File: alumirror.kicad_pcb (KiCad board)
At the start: 2 copper layers, 152.4 x 90.3 mm, 56 parts, among them SW00 PG1350, SW01 PG1350, SW02 PG1350, SW03 PG1350, SW04 PG1350, SW05 PG1350, SW10 PG1350, SW11 PG1350, SW12 PG1350, SW13 PG1350, SW14 PG1350, SW15 PG1350, SW20 PG1350, SW21 PG1350, SW22 PG1350, SW23 PG1350, SW24 PG1350, SW25 PG1350, SW30 PG1350, SW31 PG1350/SKQUCAA010, U1 CH552T, U2 CH552T

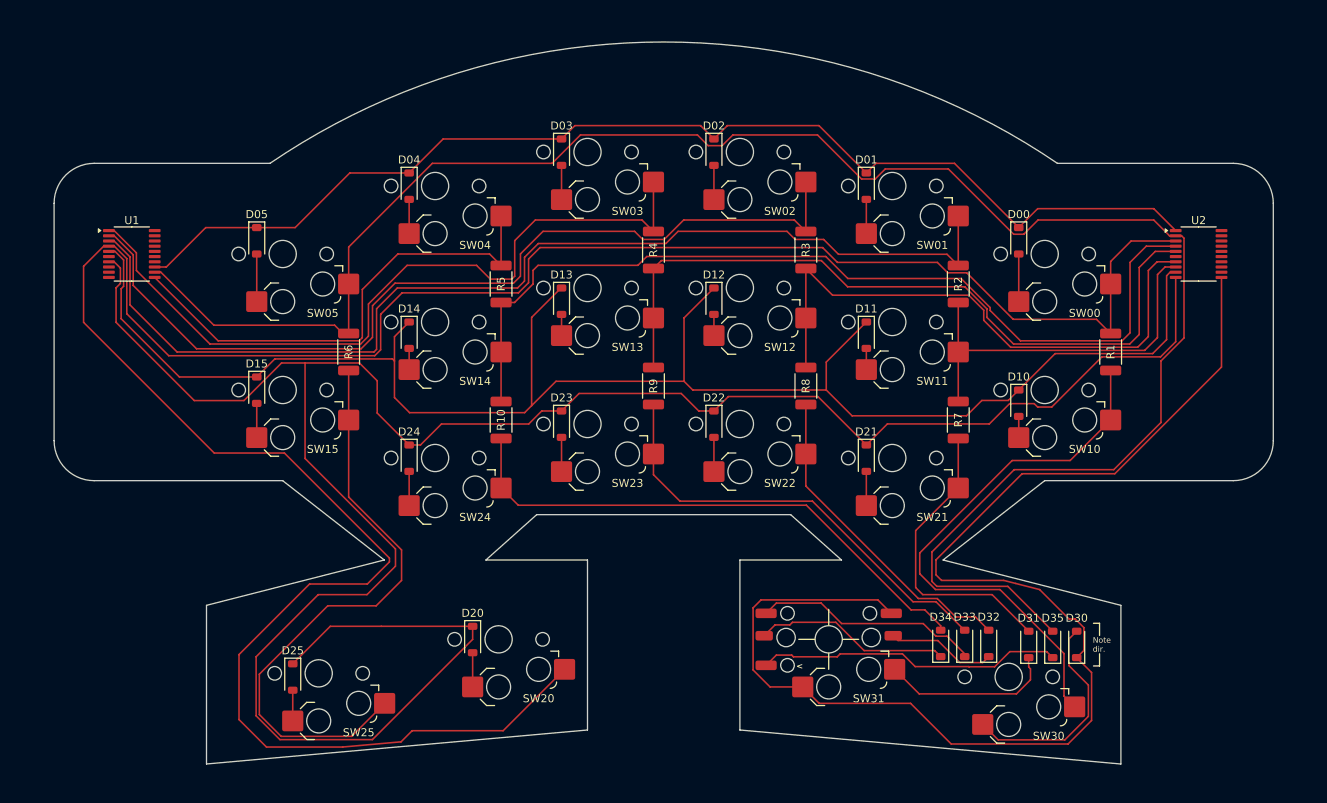
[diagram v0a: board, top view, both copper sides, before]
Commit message: Move bottom row one column over
This allows the left thumb keys to be on adjacent columns and saves routing Column 0 all the way across the board.
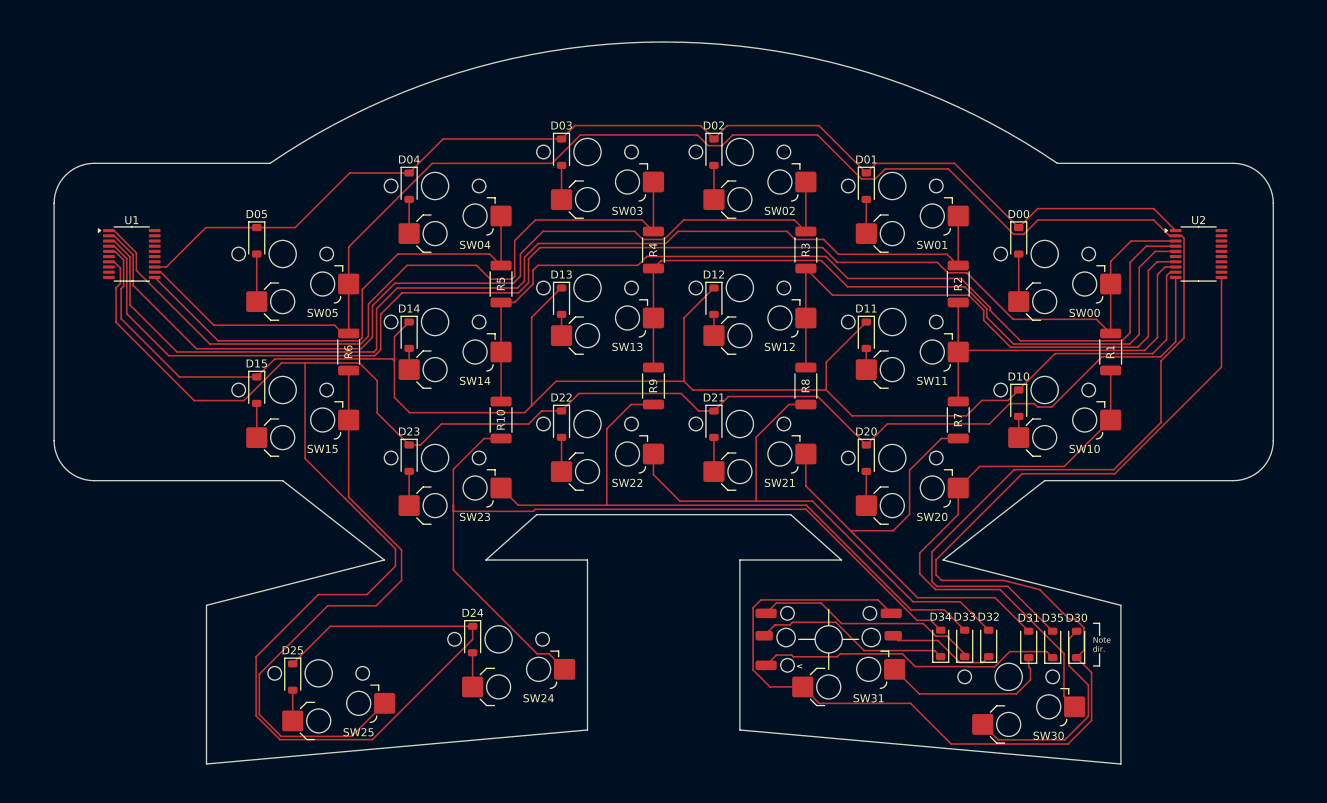
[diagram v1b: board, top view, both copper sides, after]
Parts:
- renumbered D21 to D20, D22 to D21, D23 to D22, D24 to D23, D20 to D24, SW21 to SW20, SW22 to SW21, SW23 to SW22, SW24 to SW23, SW20 to SW24
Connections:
- SW20 pad 1: /Col1R' -> /Col0'
- SW21 pad 1: /Col2R' -> /Col1R'
- SW22 pad 1: /Col3R' -> /Col2R'
- SW23 pad 1: /Col4R' -> /Col3R'
- SW24 pad 1: Col0 -> /Col4R'
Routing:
- net Col0: track 307.3 -> 167.5 mm
- net /Col4R': track 68.4 -> 107.2 mm
- net /Col2R': track 40.5 -> 68.4 mm
- net /Col3R': track 55.7 -> 82.0 mm
- net /Col1R': track 37.2 -> 60.8 mm
- net /Col0': track 68.9 -> 70.9 mm

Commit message: Tidy routing
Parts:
- moved R7 5.50 mm to (183.7, 73.2)
- moved R9 5.50 mm to (145.6, 68.9)
- moved R10 5.49 mm to (126.6, 73.2)
- moved R8 5.49 mm to (164.7, 68.9)
- moved D23 1.67 mm to (120.6, 76.3)
- moved D20 1.67 mm to (177.7, 76.3)
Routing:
- net Row2: track 293.5 -> 227.3 mm
- net /Col1R': track 60.8 -> 50.1 mm
- net /Col2R': track 68.4 -> 61.6 mm
- net /Col4R': track 107.2 -> 102.1 mm
- net /Col3R': track 82.0 -> 78.0 mm
- net /Col5': track 75.2 -> 72.1 mm
- net Col4R: track 114.7 -> 116.8 mm
- net Col3R: track 92.2 -> 94.2 mm
- net Col2R: track 72.7 -> 74.8 mm
- net Net-(D23-A): track 4.28 -> 5.95 mm
- net Net-(D20-A): track 4.28 -> 5.95 mm
- net Col1R: track 48.5 -> 50.2 mm

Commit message: Tidy schematic
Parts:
- SW25, SW30: value PG1350 -> PG1350_1½U
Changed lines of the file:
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@@
 			)
 		)
-		(property "Value" "PG1350"
+		(property "Value" "PG1350_1½U"
 			(at 0 0 180)
 			(layer "F.Fab")
@@
 			)
 		)
-		(property "Value" "PG1350"
+		(property "Value" "PG1350_1½U"
 			(at 0 0 180)
 			(layer "F.Fab")

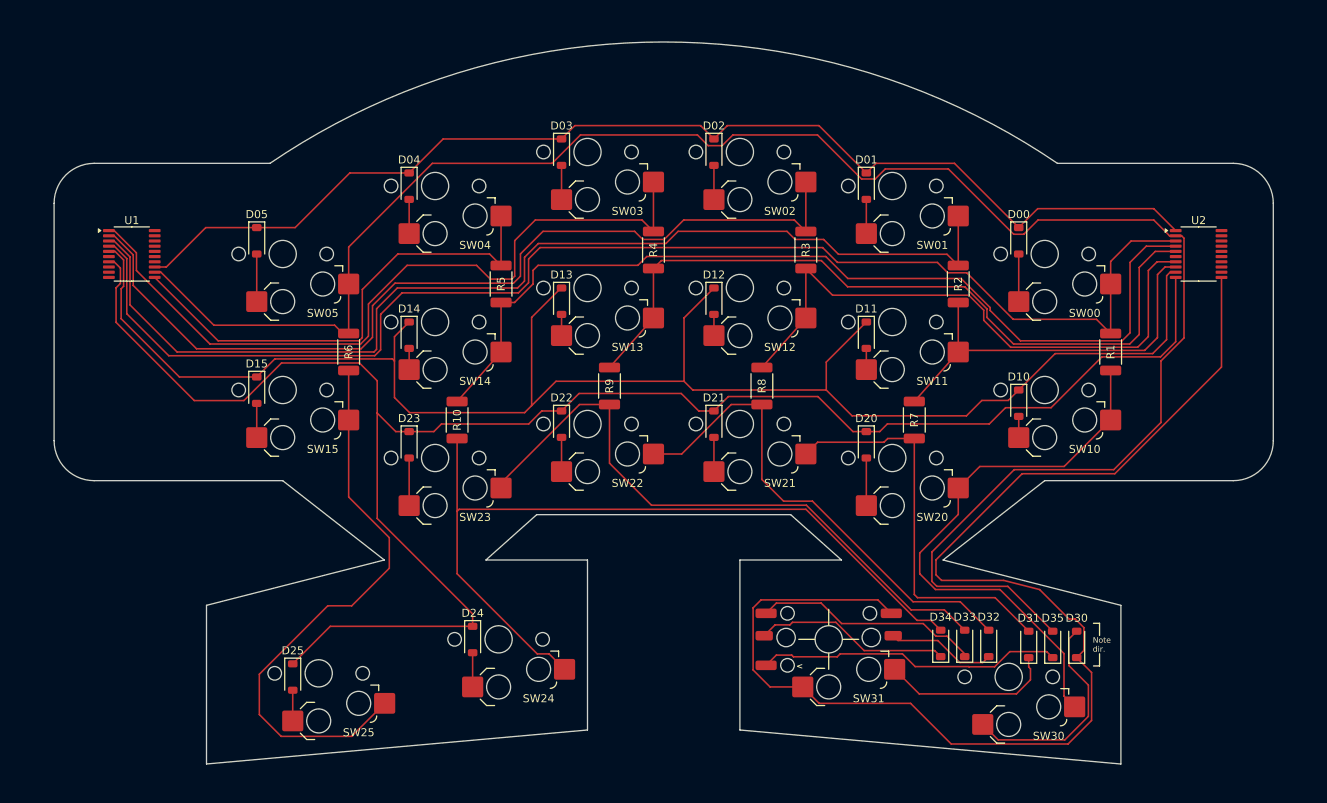
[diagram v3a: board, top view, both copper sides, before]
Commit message: Add lefthand active components to PCB and route
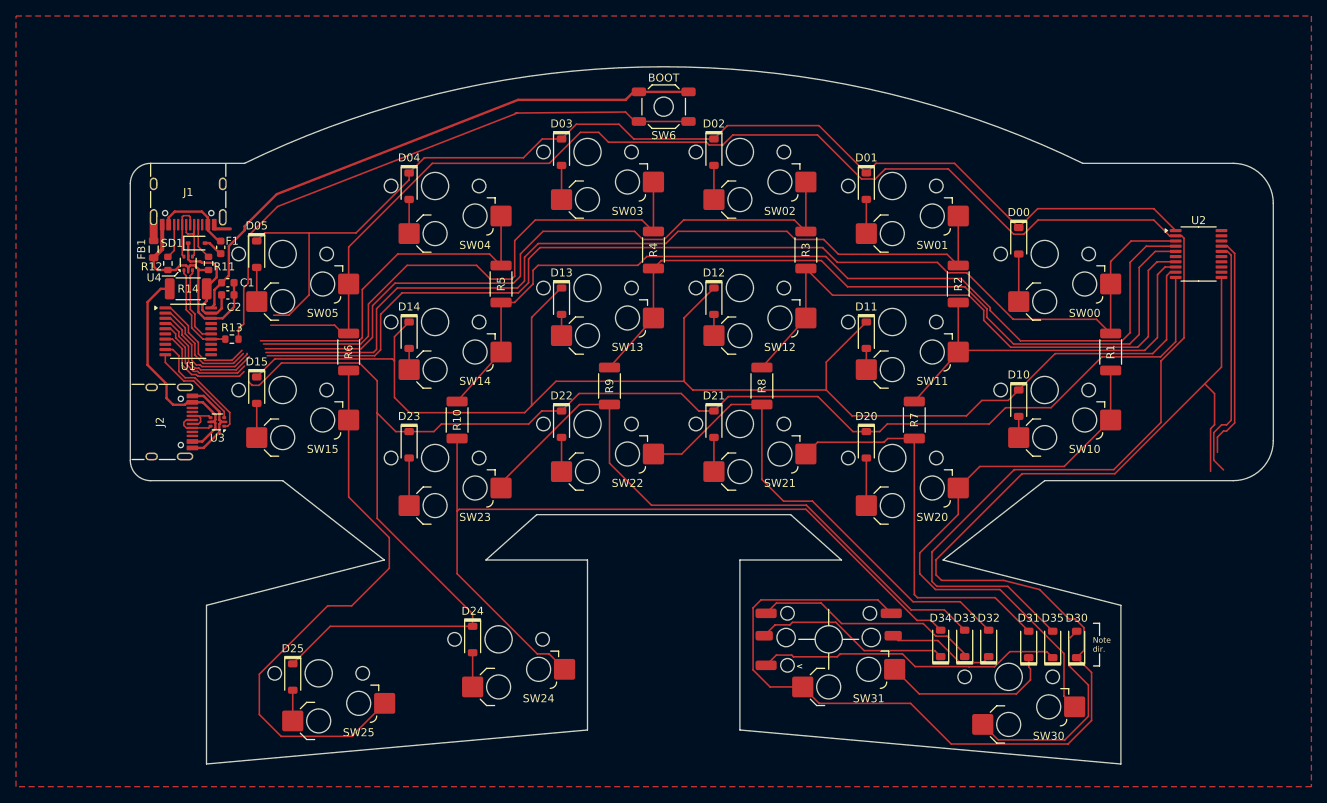
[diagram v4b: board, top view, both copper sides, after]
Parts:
- added C1: 100nF, Capacitor_SMD:C_0603_1608Metric, F.Cu at (97.9, 56.0)
- added C2: 100nF, Capacitor_SMD:C_0603_1608Metric, F.Cu at (97.9, 57.5)
- added F1: 500mA, Fuse:Fuse_0603_1608Metric, F.Cu at (97.0, 51.6)
- added FB1: FerriteBead, Inductor_SMD:L_0805_2012Metric, F.Cu at (88.6, 51.8)
- added J1: USB_C_Receptacle_USB2.0_16P_2SH, Project Library:USB_C_Receptacle_HRO_TYPE-C-31-M-12, F.Cu at (93.0, 44.7)
- added J2: USB_C_Receptacle_USB2.0_16P_2SH, Project Library:USB_C_Receptacle_HRO_TYPE-C-31-M-12, F.Cu at (89.4, 73.4)
- added NT1: NetTie_2, Project Library:NetTie-2_SMD_Pad0.2mm, F.Cu at (96.7, 63.1)
- added R11: 5k1, Resistor_SMD:R_0603_1608Metric, F.Cu at (95.5, 53.6)
- added R12: 5k1, Resistor_SMD:R_0603_1608Metric, F.Cu at (90.4, 53.6)
- added R13: 10k, Resistor_SMD:R_0603_1608Metric, F.Cu at (98.4, 63.1)
- added R14: 0R, Project Library:R_2010_5025Metric_Mod, F.Cu at (93.0, 56.8)
- added SD1: PMEG2010EA, Diode_SMD:D_SOD-323, F.Cu at (94.0, 51.1)
- added SW6: BOOT, Project Library:SW_SPST_SKQG_WithStem, F.Cu at (152.4, 34.0)
- added U3: USBLC6-2P6, Package_TO_SOT_SMD:SOT-666, F.Cu at (96.6, 73.4)
- added U4: USBLC6-2P6, Package_TO_SOT_SMD:SOT-666, F.Cu at (93.0, 53.6)
- moved U1 12.0 mm to (93.0, 62.1)
- moved D05 1.67 mm to (101.5, 52.4)
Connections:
- U1 pad 14: unconnected-(U1-P3.6/UDP-Pad14) -> USB_L+
- U1 pad 15: unconnected-(U1-P3.7/UDM-Pad15) -> USB_L-
- U1 pad 18: unconnected-(U1-GND-Pad18) -> GND
- U1 pad 19: unconnected-(U1-VCC-Pad19) -> VCC_L
- U1 pad 20: unconnected-(U1-V33-Pad20) -> +3V3_L
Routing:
- net Net-(R13-Pad2): track 0.00 -> 72.9 mm
- net +3V3_L: track 0.00 -> 71.7 mm
- net GND: track 0.00 -> 41.1 mm
- net VCC_L': track 0.00 -> 30.0 mm
- net TX_R: track 0.00 -> 30.0 mm
- net RX_R: track 0.00 -> 28.0 mm
- net Col5: track 238.1 -> 221.1 mm
- net Row2: track 227.3 -> 210.5 mm
- net VCC_L: track 0.00 -> 16.7 mm
- net Col4L: track 61.4 -> 44.9 mm
- net Row1: track 212.2 -> 196.4 mm
- net TX_L: track 0.00 -> 14.7 mm
- net Col0: track 167.5 -> 153.1 mm
- net Col1L: track 134.3 -> 120.5 mm
- net Col2L: track 113.5 -> 100.0 mm
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- added copper zone on F.Cu, net GND
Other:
- board size 152.4 x 90.3 mm -> 142.9 x 87.2 mm

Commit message: Renamed all key switches to K##
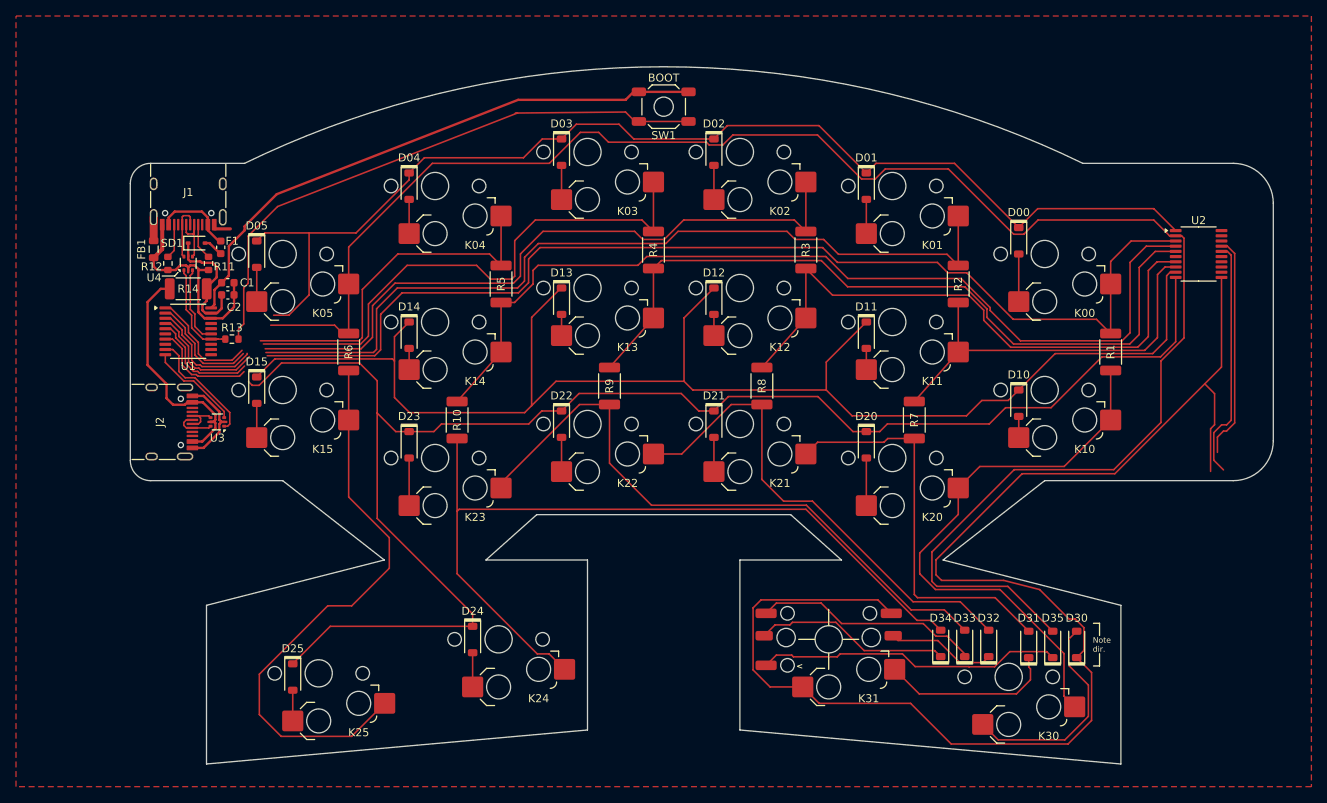
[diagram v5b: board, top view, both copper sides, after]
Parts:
- renumbered SW00 to K00, SW01 to K01, SW02 to K02, SW03 to K03, SW04 to K04, SW05 to K05, SW10 to K10, SW11 to K11, SW12 to K12, SW13 to K13, SW14 to K14, SW15 to K15, SW20 to K20, SW21 to K21, SW22 to K22, SW23 to K23, SW24 to K24, SW25 to K25, SW30 to K30, SW31 to K31, SW6 to SW1
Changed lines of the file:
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@@
 		(at 104.775 69.416683)
 		(descr "Hotswap footprint for Kailh Choc style switches")
-		(property "Reference" "SW15"
+		(property "Reference" "K15"
 			(at 5 7.4 180)
 			(layer "F.SilkS")
@@
 		(at 123.825 77.916684)
 		(descr "Hotswap footprint for Kailh Choc style switches")
-		(property "Reference" "SW23"
+		(property "Reference" "K23"
 			(at 5 7.4 180)
 			(layer "F.SilkS")
@@
 		(at 180.975 43.916677)
 		(descr "Hotswap footprint for Kailh Choc style switches")
-		(property "Reference" "SW01"
+		(property "Reference" "K01"
 			(at 5 7.4 180)
 			(layer "F.SilkS")
@@
 		(at 195.525 105.272109)
 		(descr "Hotswap footprint for Kailh Choc style switches")
-		(property "Reference" "SW30"
+		(property "Reference" "K30"
 			(at 5 7.4 180)
 			(layer "F.SilkS")
@@
 		(at 142.875 56.66668)
 		(descr "Hotswap footprint for Kailh Choc style switches")
-		(property "Reference" "SW13"
+		(property "Reference" "K13"
 			(at 5 7.4 180)
 			(layer "F.SilkS")
@@
 		(tags "capacitor")
 		(property "Reference" "C1"
-			(at 2.413 0 360)
+			(at 2.413 0 0)
 			(layer "F.SilkS")
 			(effects
@@
 		)
 		(property "Value" "100nF"
-			(at 0 1.43 360)
+			(at 0 1.43 0)
 			(layer "F.Fab")
 			(effects
@@
 		)
 		(fp_text user "${REFERENCE}"
-			(at 0 0 360)
+			(at 0 0 0)
 			(layer "F.Fab")
 			(effects
@@
 		(at 123.825 60.916681)
 		(descr "Hotswap footprint for Kailh Choc style switches")
-		(property "Reference" "SW14"
+		(property "Reference" "K14"
 			(at 5 7.4 180)
 			(layer "F.SilkS")
@@
 		(at 200.025 69.416683)
 		(descr "Hotswap footprint for Kailh Choc style switches")
-		(property "Reference" "SW10"
+		(property "Reference" "K10"
 			(at 5 7.4 180)
 			(layer "F.SilkS")
@@
 		(tags "resistor")
 		(property "Reference" "R13"
-			(at 0 -1.43 360)
+			(at 0 -1.43 0)
 			(layer "F.SilkS")
 			(effects
@@
 		)
 		(property "Value" "10k"
-			(at 0 1.43 360)
+			(at 0 1.43 0)
 			(layer "F.Fab")
 			(effects
@@
 		)
 		(fp_text user "${REFERENCE}"
-			(at 0 0 360)
+			(at 0 0 0)
 			(layer "F.Fab")
 			(effects
@@
 		(at 104.775 52.416679)
 		(descr "Hotswap footprint for Kailh Choc style switches")
-		(property "Reference" "SW05"
+		(property "Reference" "K05"
 			(at 5 7.4 180)
 			(layer "F.SilkS")
@@
 		(at 200.025 52.416679)
 		(descr "Hotswap footprint for Kailh Choc style switches")
-		(property "Reference" "SW00"
+		(property "Reference" "K00"
 			(at 5 7.4 180)
 			(layer "F.SilkS")
@@
 		(at 180.975 77.916685)
 		(descr "Hotswap footprint for Kailh Choc style switches")
-		(property "Reference" "SW20"
+		(property "Reference" "K20"
 			(at 5 7.4 180)
 			(layer "F.SilkS")
@@
 		(at 131.7625 100.583357)
 		(descr "Hotswap footprint for Kailh Choc style switches")
-		(property "Reference" "SW24"
+		(property "Reference" "K24"
 			(at 5 7.4 180)
 			(layer "F.SilkS")
@@
 		(at 109.275 104.833358)
 		(descr "Hotswap footprint for Kailh Choc style switches")
-		(property "Reference" "SW25"
+		(property "Reference" "K25"
 			(at 5 7.4 180)
 			(layer "F.SilkS")
@@
 		(at 142.875 73.666684)
 		(descr "Hotswap footprint for Kailh Choc style switches")
-		(property "Reference" "SW22"
+		(property "Reference" "K22"
 			(at 5 7.4 180)
 			(layer "F.SilkS")
@@
 		(at 180.975 60.916681)
 		(descr "Hotswap footprint for Kailh Choc style switches")
-		(property "Reference" "SW11"
+		(property "Reference" "K11"
 			(at 5 7.4 180)
 			(layer "F.SilkS")
@@
 		(tags "capacitor")
 		(property "Reference" "C2"
-			(at 0.775 1.524 360)
+			(at 0.775 1.524 0)
 			(layer "F.SilkS")
 			(effects
@@
 		)
 		(property "Value" "100nF"
-			(at 0 1.43 360)
+			(at 0 1.43 0)
 			(layer "F.Fab")
 			(effects
@@
 		)
 		(fp_text user "${REFERENCE}"
-			(at 0 0 360)
+			(at 0 0 0)
 			(layer "F.Fab")
 			(effects
@@
 		(at 123.825 43.916677)
 		(descr "Hotswap footprint for Kailh Choc style switches")
-		(property "Reference" "SW04"
+		(property "Reference" "K04"
 			(at 5 7.4 180)
 			(layer "F.SilkS")
@@
 		(at 173.025 100.583357)
 		(descr "Hotswap footprint for Kailh Choc style switches")
-		(property "Reference" "SW31"
+		(property "Reference" "K31"
 			(at 5 7.4 180)
 			(layer "F.SilkS")
@@
 		(descr "ALPS 5.2mm Square Low-profile Type (Surface Mount) SKQG Series, With stem, http://www.alps.com/prod/info/E/HTML/Tact/SurfaceMount/SKQG/SKQGAFE010.html")
 		(tags "SPST Button Switch")
-		(property "Reference" "SW6"
+		(property "Reference" "SW1"
 			(at 0 -3.6 180)
 			(layer "F.SilkS")
@@
 		(at 161.925 39.666676)
 		(descr "Hotswap footprint for Kailh Choc style switches")
-		(property "Reference" "SW02"
+		(property "Reference" "K02"
 			(at 5 7.4 180)
 			(layer "F.SilkS")
@@
 		(at 161.925 56.66668)
 		(descr "Hotswap footprint for Kailh Choc style switches")
-		(property "Reference" "SW12"
+		(property "Reference" "K12"
 			(at 5 7.4 180)
 			(layer "F.SilkS")
@@
 		(at 161.925 73.666684)
 		(descr "Hotswap footprint for Kailh Choc style switches")
-		(property "Reference" "SW21"
+		(property "Reference" "K21"
 			(at 5 7.4 180)
 			(layer "F.SilkS")
@@
 		(at 142.875 39.666676)
 		(descr "Hotswap footprint for Kailh Choc style switches")
-		(property "Reference" "SW03"
+		(property "Reference" "K03"
 			(at 5 7.4 180)
 			(layer "F.SilkS")
